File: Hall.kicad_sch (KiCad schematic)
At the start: 5 parts, among them J1 Conn_01x03_Pin

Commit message: Add files via upload
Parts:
- C1: footprint Capacitor_SMD:C_0201_0603Metric -> Capacitor_SMD:C_0603_1608Metric
- C2: footprint Capacitor_SMD:C_0201_0603Metric_Pad0.64x0.40mm_HandSolder -> Capacitor_SMD:C_0603_1608Metric
- R1: footprint Resistor_SMD:R_0201_0603Metric -> Resistor_SMD:R_0603_1608Metric
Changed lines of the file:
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@@
       (effects (font (size 1.27 1.27)))
     )
-    (property "Footprint" "Resistor_SMD:R_0201_0603Metric" (at 109.22 71.628 90)
+    (property "Footprint" "Resistor_SMD:R_0603_1608Metric" (at 109.22 71.628 90)
       (effects (font (size 1.27 1.27)) hide)
     )
@@
       (effects (font (size 1.27 1.27)) (justify left))
     )
-    (property "Footprint" "Capacitor_SMD:C_0201_0603Metric_Pad0.64x0.40mm_HandSolder" (at 103.8352 77.47 0)
+    (property "Footprint" "Capacitor_SMD:C_0603_1608Metric" (at 103.8352 77.47 0)
       (effects (font (size 1.27 1.27)) hide)
     )
@@
       (effects (font (size 1.27 1.27)))
     )
-    (property "Footprint" "Capacitor_SMD:C_0201_0603Metric" (at 107.95 63.8048 0)
-      (effects (font (size 1.27 1.27)) hide)
-    )
+    (property "Footprint" "Capacitor_SMD:C_0603_1608Metric" (at 107.95 63.8048 0)
+      (effects (font (size 1.27 1.27)) hide)
+    )

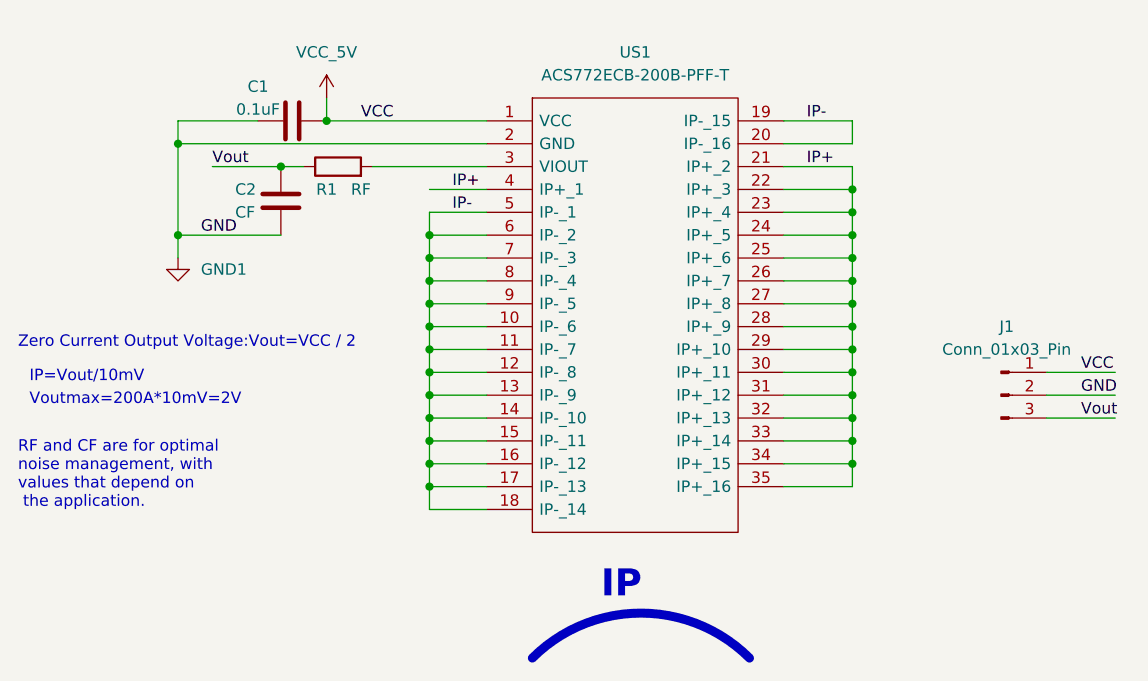
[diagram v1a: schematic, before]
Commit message: Add files via upload
Add a voltage divider resistor for AD detection to enable the external 3.3V MCU to directly read the AD value.
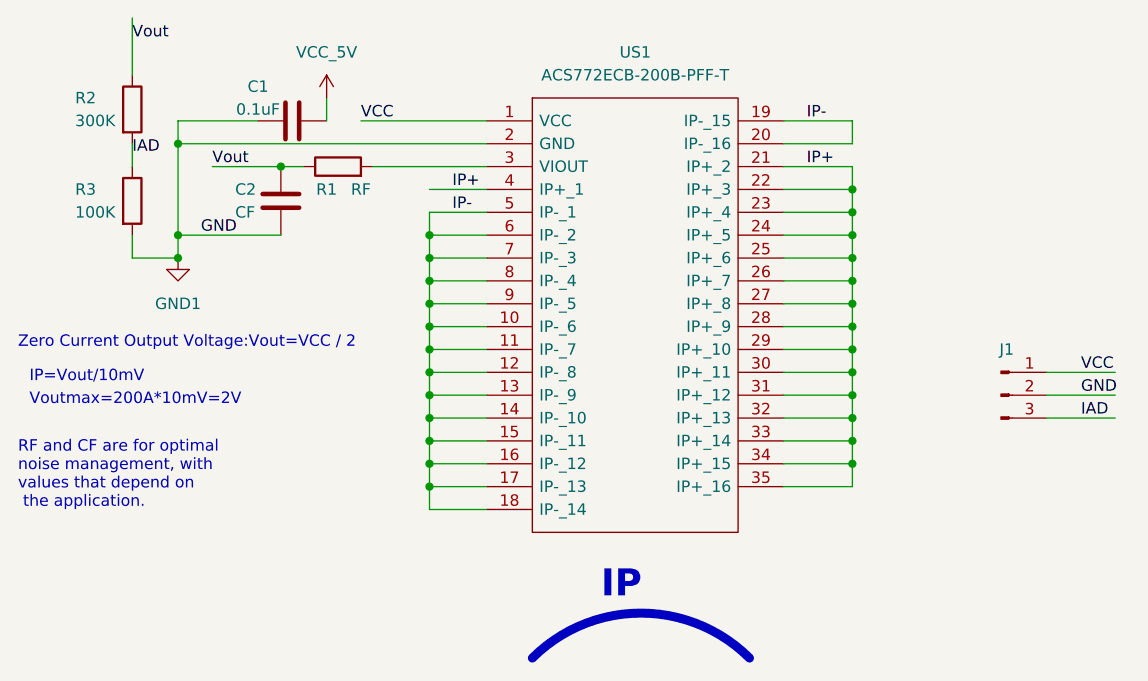
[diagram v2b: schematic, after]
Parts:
- added R2: 300K, Resistor_SMD:R_0603_1608Metric, symbol Device:R
- added R3: 100K, Resistor_SMD:R_0603_1608Metric, symbol Device:R
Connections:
- net GND1: now also R3.2
- net Vout: now also R2.1; no longer J1.3 (Pin_3)
- new net IAD: J1.3 (Pin_3), R2.2, R3.1
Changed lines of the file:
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@@
   (junction (at 119.38 92.71) (diameter 0) (color 0 0 0 0)
   )
-  (junction (at 107.95 64.77) (diameter 0) (color 0 0 0 0)
-  )
   (junction (at 166.37 80.01) (diameter 0) (color 0 0 0 0)
   )
@@
   (junction (at 119.38 97.79) (diameter 0) (color 0 0 0 0)
   )
+  (junction (at 91.44 80.01) (diameter 0) (color 0 0 0 0)
+  )
   (junction (at 166.37 74.93) (diameter 0) (color 0 0 0 0)
   )
@@
     (stroke (width 0) (type default))
   )
+  (wire (pts (xy 86.36 80.01) (xy 91.44 80.01))
+    (stroke (width 0) (type default))
+  )
   (wire (pts (xy 91.44 77.47) (xy 91.44 67.31))
     (stroke (width 0) (type default))
@@
     (stroke (width 0) (type default))
   )
+  (wire (pts (xy 86.36 67.31) (xy 86.36 69.85))
+    (stroke (width 0) (type default))
+  )
   (wire (pts (xy 166.37 72.39) (xy 166.37 74.93))
     (stroke (width 0) (type default))
@@
     (stroke (width 0) (type default))
   )
+  (wire (pts (xy 111.76 64.77) (xy 125.73 64.77))
+    (stroke (width 0) (type default))
+  )
   (wire (pts (xy 187.96 92.71) (xy 195.58 92.71))
     (stroke (width 0) (type default))
@@
     (stroke (width 0) (type default))
   )
+  (wire (pts (xy 86.36 53.34) (xy 86.36 59.69))
+    (stroke (width 0) (type default))
+  )
   (wire (pts (xy 166.37 102.87) (xy 166.37 105.41))
     (stroke (width 0) (type default))
@@
     (stroke (width 0) (type default))
   )
+  (wire (pts (xy 86.36 77.47) (xy 86.36 80.01))
+    (stroke (width 0) (type default))
+  )
   (wire (pts (xy 119.38 82.55) (xy 125.73 82.55))
     (stroke (width 0) (type default))
@@
   )
   (wire (pts (xy 102.87 69.85) (xy 105.41 69.85))
-    (stroke (width 0) (type default))
-  )
-  (wire (pts (xy 125.73 64.77) (xy 107.95 64.77))
     (stroke (width 0) (type default))
   )
@@
     (effects (font (size 1.27 1.27)) (justify left bottom))
   )
+  (label "IAD" (at 86.36 68.58 0) (fields_autoplaced)
+    (effects (font (size 1.27 1.27)) (justify left bottom))
+  )
   (label "IP-" (at 161.29 64.77 0) (fields_autoplaced)
     (effects (font (size 1.27 1.27)) (justify left bottom))
@@
     (effects (font (size 1.27 1.27)) (justify left bottom))
   )
+  (label "Vout" (at 86.36 55.88 0) (fields_autoplaced)
+    (effects (font (size 1.27 1.27) (color 255 3 26 1)) (justify left bottom))
+  )
   (label "IP+" (at 161.29 69.85 0) (fields_autoplaced)
     (effects (font (size 1.27 1.27)) (justify left bottom))
   )
-  (label "Vout" (at 191.77 97.79 0) (fields_autoplaced)
+  (label "IAD" (at 191.77 97.79 0) (fields_autoplaced)
     (effects (font (size 1.27 1.27) (color 255 3 26 1)) (justify left bottom))
+  )
+  (symbol (lib_id "Device:R") (at 86.36 63.5 0) (unit 1)
+    (in_bom yes) (on_board yes) (dnp no)
+    (property "Reference" "R2" (at 80.01 62.23 0)
+      (effects (font (size 1.27 1.27)) (justify left))
+    )
+    (property "Value" "300K" (at 80.01 64.77 0)
+      (effects (font (size 1.27 1.27)) (justify left))
+    )
+    (property "Footprint" "Resistor_SMD:R_0603_1608Metric" (at 84.582 63.5 90)
+      (effects (font (size 1.27 1.27)) hide)
+    )
+    (property "Datasheet" "~" (at 86.36 63.5 0)
+      (effects (font (size 1.27 1.27)) hide)
+    )
+    (pin "1")
+    (pin "2")
+    (instances
+      (project "Hall"
+        (path "/b3060d4e-7467-4a22-9473-769120214355"
+          (reference "R2") (unit 1)
+        )
+      )
+    )
+  )
+  (symbol (lib_id "Device:R") (at 86.36 73.66 0) (unit 1)
+    (in_bom yes) (on_board yes) (dnp no)
+    (property "Reference" "R3" (at 80.01 72.39 0)
+      (effects (font (size 1.27 1.27)) (justify left))
+    )
+    (property "Value" "100K" (at 80.01 74.93 0)
+      (effects (font (size 1.27 1.27)) (justify left))
+    )
+    (property "Footprint" "Resistor_SMD:R_0603_1608Metric" (at 84.582 73.66 90)
+      (effects (font (size 1.27 1.27)) hide)
+    )
+    (property "Datasheet" "~" (at 86.36 73.66 0)
+      (effects (font (size 1.27 1.27)) hide)
+    )
+    (pin "1")
+    (pin "2")
+    (instances
+      (project "Hall"
+        (path "/b3060d4e-7467-4a22-9473-769120214355"
+          (reference "R3") (unit 1)
+        )
+      )
+    )
   )
   (symbol (lib_id "Connector:Conn_01x03_Pin") (at 182.88 95.25 0) (unit 1)
     (in_bom yes) (on_board yes) (dnp no) (fields_autoplaced)
-    (property "Reference" "J1" (at 183.515 87.63 0)
+    (property "Reference" "J1" (at 183.515 90.17 0)
       (effects (font (size 1.27 1.27)))
     )
     (property "Value" "Conn_01x03_Pin" (at 183.515 90.17 0)
-      (effects (font (size 1.27 1.27)))
+      (effects (font (size 1.27 1.27)) hide)
     )
     (property "Footprint" "Connector:FanPinHeader_1x03_P2.54mm_Vertical" (at 182.88 95.25 0)
@@
       (effects (font (size 1.27 1.27)) hide)
     )
-    (property "Value" "GND1" (at 93.98 81.28 0)
-      (effects (font (size 1.27 1.27)) (justify left))
+    (property "Value" "GND1" (at 91.44 85.09 0)
+      (effects (font (size 1.27 1.27)))
     )
     (property "Footprint" "" (at 91.44 80.01 0)
